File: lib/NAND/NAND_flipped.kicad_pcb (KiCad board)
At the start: 2 copper layers, 4 parts, among them P1 Q_PJFET_GSD, P2 Q_PJFET_GSD

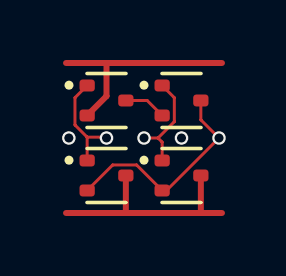
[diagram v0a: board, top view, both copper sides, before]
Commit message: Somehow NAND PCB was botched. Changed pin position of B, too
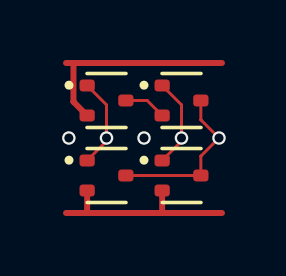
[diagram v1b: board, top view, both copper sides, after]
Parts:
- N1, N2: value Q_NJFET_GSD -> (none)
- P1, P2: value Q_PJFET_GSD -> (none)
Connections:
- net Net-(Q3-D) renamed int1
- P1 pad 2: Y -> VDD
- P1 pad 3: VDD -> Y
- P2 pad 2: Y -> VDD
- P2 pad 3: VDD -> Y
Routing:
- net Y: track 7.33 -> 5.50 mm
- net VDD: track 7.70 -> 6.72 mm
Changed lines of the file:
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@@
 	(net 3 "A")
 	(net 4 "VDD")
-	(net 5 "Net-(Q3-D)")
+	(net 5 "int1")
 	(net 6 "B")
 	(footprint "Package_TO_SOT_SMD:SOT-523"
@@
 			)
 		)
-		(property "Value" "Q_NJFET_GSD"
+		(property "Value" ""
 			(at 0 1.75 0)
 			(layer "F.Fab")
@@
 			(net 6 "B")
 			(pinfunction "G")
-			(pintype "input")
+			(pintype "inout")
 		)
 		(pad "2" smd roundrect
@@
 			(layers "F.Cu" "F.Mask" "F.Paste")
 			(roundrect_rratio 0.25)
-			(net 5 "Net-(Q3-D)")
+			(net 5 "int1")
 			(pinfunction "S")
-			(pintype "passive")
+			(pintype "inout")
 		)
 		(pad "3" smd roundrect
@@
 			(net 1 "Y")
 			(pinfunction "D")
-			(pintype "passive")
+			(pintype "inout")
 		)
 		(embedded_fonts no)
@@
 			)
 		)
-		(property "Value" "Q_PJFET_GSD"
+		(property "Value" ""
 			(at 0 1.75 0)
 			(layer "F.Fab")
@@
 			(net 6 "B")
 			(pinfunction "G")
-			(pintype "input")
+			(pintype "inout")
 		)
 		(pad "2" smd roundrect
@@
 			(layers "F.Cu" "F.Mask" "F.Paste")
 			(roundrect_rratio 0.25)
-			(net 1 "Y")
+			(net 4 "VDD")
 			(pinfunction "S")
-			(pintype "passive")
+			(pintype "inout")
 		)
 		(pad "3" smd roundrect
@@
 			(layers "F.Cu" "F.Mask" "F.Paste")
 			(roundrect_rratio 0.25)
-			(net 4 "VDD")
+			(net 1 "Y")
 			(pinfunction "D")
-			(pintype "passive")
+			(pintype "inout")
 		)
 		(embedded_fonts no)
@@
 			)
 		)
-		(property "Value" "Q_NJFET_GSD"
+		(property "Value" ""
 			(at 0 1.75 0)
 			(layer "F.Fab")
@@
 			(net 3 "A")
 			(pinfunction "G")
-			(pintype "input")
+			(pintype "inout")
 		)
 		(pad "2" smd roundrect
@@
 			(net 2 "GND")
 			(pinfunction "S")
-			(pintype "passive")
+			(pintype "inout")
 		)
 		(pad "3" smd roundrect
@@
 			(layers "F.Cu" "F.Mask" "F.Paste")
 			(roundrect_rratio 0.25)
-			(net 5 "Net-(Q3-D)")
+			(net 5 "int1")
 			(pinfunction "D")
-			(pintype "passive")
+			(pintype "inout")
 		)
 		(embedded_fonts no)
@@
 			)
 		)
-		(property "Value" "Q_PJFET_GSD"
+		(property "Value" ""
 			(at 0 1.75 0)
 			(layer "F.Fab")
@@
 			(net 3 "A")
 			(pinfunction "G")
-			(pintype "input")
+			(pintype "inout")
 		)
 		(pad "2" smd roundrect
@@
 			(layers "F.Cu" "F.Mask" "F.Paste")
 			(roundrect_rratio 0.25)
-			(net 1 "Y")
+			(net 4 "VDD")
 			(pinfunction "S")
-			(pintype "passive")
+			(pintype "inout")
 		)
 		(pad "3" smd roundrect
@@
 			(layers "F.Cu" "F.Mask" "F.Paste")
 			(roundrect_rratio 0.25)
-			(net 4 "VDD")
+			(net 1 "Y")
 			(pinfunction "D")
-			(pintype "passive")
+			(pintype "inout")
 		)
 		(embedded_fonts no)
@@
 			)
 		)
-	)
-	(via
-		(at 3.75 2.5)
-		(size 0.45)
-		(drill 0.3)
-		(layers "F.Cu" "B.Cu")
-		(net 0)
 	)
 	(via
@@
 		(net 0)
 	)
+	(via
+		(at 2.5 2.5)
+		(size 0.45)
+		(drill 0.3)
+		(layers "F.Cu" "B.Cu")
+		(net 0)
+	)
 	(segment
 		(start 4.395 1.895)
-		(end 4.395 1.25)
+		(end 5 2.5)
 		(width 0.1)
 		(layer "F.Cu")
@@
 	)
 	(segment
-		(start 3.25 4.25)
-		(end 5 2.5)
+		(start 4.395 1.25)
+		(end 4.395 1.895)
 		(width 0.1)
 		(layer "F.Cu")
@@
 	(segment
 		(start 5 2.5)
-		(end 4.395 1.895)
+		(end 4.395 3.105)
 		(width 0.1)
 		(layer "F.Cu")
@@
 	)
 	(segment
-		(start 2.254 3.399)
-		(end 3.105 4.25)
+		(start 4.395 3.105)
+		(end 4.395 3.75)
 		(width 0.1)
 		(layer "F.Cu")
@@
 	)
 	(segment
-		(start 1.456 3.399)
-		(end 2.254 3.399)
-		(width 0.1)
-		(layer "F.Cu")
-		(net 1)
-	)
-	(segment
-		(start 3.105 4.25)
-		(end 3.25 4.25)
-		(width 0.1)
-		(layer "F.Cu")
-		(net 1)
-	)
-	(segment
-		(start 0.605 4.25)
-		(end 1.456 3.399)
+		(start 4.395 3.75)
+		(end 1.895 3.75)
 		(width 0.1)
 		(layer "F.Cu")
@@
 	)
 	(segment
-		(start 1.25 1.105)
-		(end 1.25 0)
+		(start 0.605 1.75)
+		(end 0.149 1.294)
+		(width 0.2)
+		(layer "F.Cu")
+		(net 2)
+	)
+	(segment
+		(start -0.1 0)
+		(end 0.2 0)
 		(width 0.2)
 		(layer "F.Cu")
@@
 	)
 	(segment
-		(start -0.1 0)
+		(start 0.2 0)
 		(end 1.25 0)
 		(width 0.2)
@@
 	)
 	(segment
-		(start 0.605 1.75)
-		(end 1.25 1.105)
+		(start 0.149 1.294)
+		(end 0.149 0.051)
 		(width 0.2)
 		(layer "F.Cu")
@@
 	)
 	(segment
-		(start 0.605 2.472189)
-		(end 1.222189 2.472189)
+		(start 0.149 0.051)
+		(end 0.2 0)
+		(width 0.2)
+		(layer "F.Cu")
+		(net 2)
+	)
+	(segment
+		(start 0.605 0.75)
+		(end 1.25 1.395)
 		(width 0.1)
 		(layer "F.Cu")
@@
 	)
 	(segment
-		(start 1.222189 2.472189)
+		(start 1.25 1.395)
 		(end 1.25 2.5)
 		(width 0.1)
@@
 	)
 	(segment
-		(start 0.199 2.066189)
-		(end 0.605 2.472189)
+		(start 1.25 2.605)
+		(end 0.605 3.25)
 		(width 0.1)
 		(layer "F.Cu")
@@
 	)
 	(segment
-		(start 0.199 1.156)
-		(end 0.199 2.066189)
-		(width 0.1)
-		(layer "F.Cu")
-		(net 3)
-	)
-	(segment
-		(start 0.605 0.75)
-		(end 0.199 1.156)
-		(width 0.1)
-		(layer "F.Cu")
-		(net 3)
-	)
-	(segment
-		(start 0.605 2.472189)
-		(end 0.605 3.25)
+		(start 1.25 2.5)
+		(end 1.25 2.605)
 		(width 0.1)
 		(layer "F.Cu")
@@
 	(segment
 		(start -0.1 5)
-		(end 1.9 5)
+		(end 0.65 5)
 		(width 0.2)
 		(layer "F.Cu")
@@
 	(segment
 		(start 1.9 5)
+		(end 3.1 5)
+		(width 0.2)
+		(layer "F.Cu")
+		(net 4)
+	)
+	(segment
+		(start 0.605 4.25)
+		(end 0.605 4.955)
+		(width 0.2)
+		(layer "F.Cu")
+		(net 4)
+	)
+	(segment
+		(start 0.605 4.955)
+		(end 0.65 5)
+		(width 0.2)
+		(layer "F.Cu")
+		(net 4)
+	)
+	(segment
+		(start 0.65 5)
+		(end 1.9 5)
+		(width 0.2)
+		(layer "F.Cu")
+		(net 4)
+	)
+	(segment
+		(start 3.1 5)
 		(end 4.4 5)
 		(width 0.2)
@@
 	)
 	(segment
-		(start 1.895 4.995)
-		(end 1.9 5)
+		(start 3.105 4.995)
+		(end 3.1 5)
 		(width 0.2)
 		(layer "F.Cu")
@@
 	)
 	(segment
-		(start 4.395 3.75)
-		(end 4.395 4.995)
-		(width 0.2)
-		(layer "F.Cu")
-		(net 4)
-	)
-	(segment
-		(start 4.395 4.995)
-		(end 4.4 5)
-		(width 0.2)
-		(layer "F.Cu")
-		(net 4)
-	)
-	(segment
-		(start 1.895 3.75)
-		(end 1.895 4.995)
+		(start 3.105 4.25)
+		(end 3.105 4.995)
 		(width 0.2)
 		(layer "F.Cu")
@@
 	)
 	(segment
-		(start 3.105 2.637262)
-		(end 2.967738 2.5)
+		(start 3.75 2.5)
+		(end 3.75 2.605)
 		(width 0.1)
 		(layer "F.Cu")
@@
 	)
 	(segment
-		(start 3.105 3.25)
-		(end 3.105 2.637262)
+		(start 3.75 1.395)
+		(end 3.75 2.5)
 		(width 0.1)
 		(layer "F.Cu")
@@
 	)
 	(segment
-		(start 3.511 1.956738)
-		(end 2.967738 2.5)
+		(start 3.105 0.75)
+		(end 3.75 1.395)
 		(width 0.1)
 		(layer "F.Cu")
@@
 	)
 	(segment
-		(start 3.511 1.156)
-		(end 3.511 1.956738)
+		(start 3.75 2.605)
+		(end 3.105 3.25)
 		(width 0.1)
 		(layer "F.Cu")
 		(net 6)
 	)
-	(segment
-		(start 3.105 0.75)
-		(end 3.511 1.156)
-		(width 0.1)
-		(layer "F.Cu")
-		(net 6)
-	)
-	(segment
-		(start 2.967738 2.5)
-		(end 2.5 2.5)
-		(width 0.1)
-		(layer "F.Cu")
-		(net 6)
-	)
 	(via
-		(at 2.5 2.5)
+		(at 3.75 2.5)
 		(size 0.45)
 		(drill 0.3)

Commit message: High-density layout with pitch of 1.1mm, which gains 23% !!
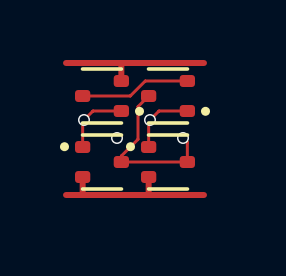
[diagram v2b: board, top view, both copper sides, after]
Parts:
- moved P2 0.64 mm to (3.30, 3.30)
- moved N2 0.47 mm to (3.30, 1.10), turned to 180 degrees
- moved P1 0.47 mm to (1.10, 3.30)
- moved N1 0.21 mm to (1.10, 1.10), turned to 180 degrees
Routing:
- net int1: track 1.42 -> 3.70 mm
- net GND: track 7.16 -> 5.20 mm
- net VDD: track 6.72 -> 5.80 mm
- net B: track 3.03 -> 2.29 mm
- net A: track 3.03 -> 2.29 mm
- net (no net): vias 2 -> 1
